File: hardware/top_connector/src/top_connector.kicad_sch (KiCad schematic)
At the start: 13 parts, among them J1 to prev top connector, J2 to next top connector, J3 to module, U1 XL1509-5.0, U2 74LVC1G66

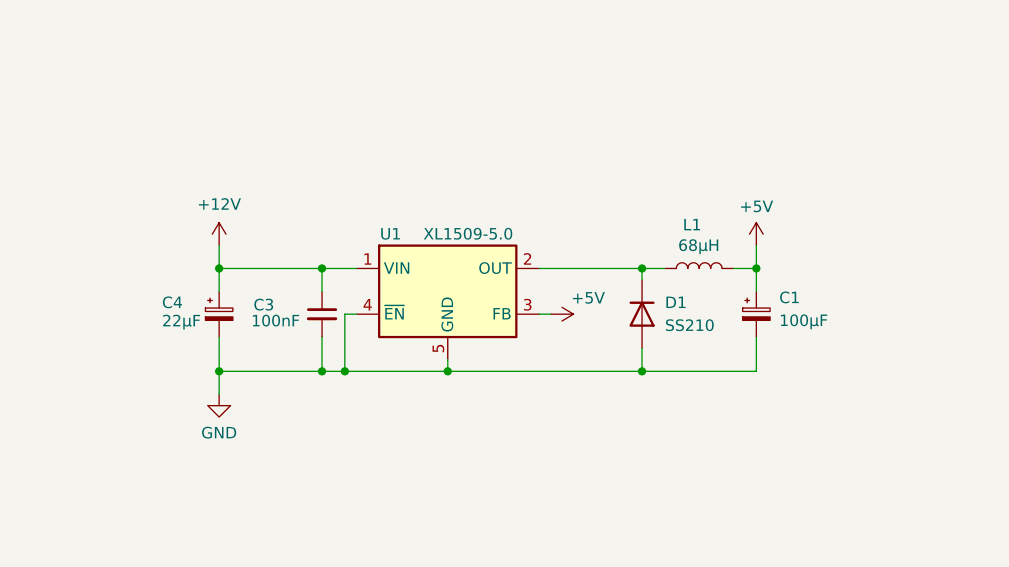
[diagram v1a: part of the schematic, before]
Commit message: Changed micro symbol to uF
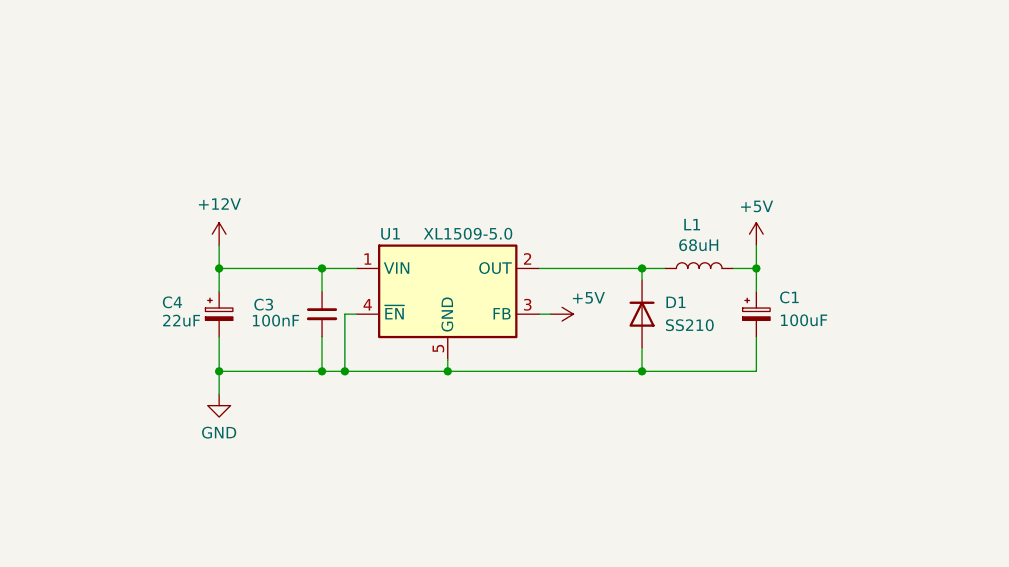
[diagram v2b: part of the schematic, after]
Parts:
- C1: value 100µF -> 100uF
- C4: value 22µF -> 22uF
- L1: value 68µH -> 68uH
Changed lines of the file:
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@@
 		(rev "2.0.1")
 		(company "OpenFlap")
-        (comment 1 "${GIT_TAG}")
+		(comment 1 "${GIT_TAG}")
 		(comment 2 "Repo: github.com/ToonVanEyck/OpenFlap")
 		(comment 3 "Designer: Toon Van Eyck")
@@
 			)
 		)
-		(property "Value" "22µF"
+		(property "Value" "22uF"
 			(at 69.85 201.422 0)
 			(effects
@@
 			)
 		)
-		(property "Value" "68µH"
+		(property "Value" "68uH"
 			(at 131.826 193.04 90)
 			(effects
@@
 			)
 		)
-		(property "Value" "100µF"
+		(property "Value" "100uF"
 			(at 138.43 201.3839 0)
 			(effects

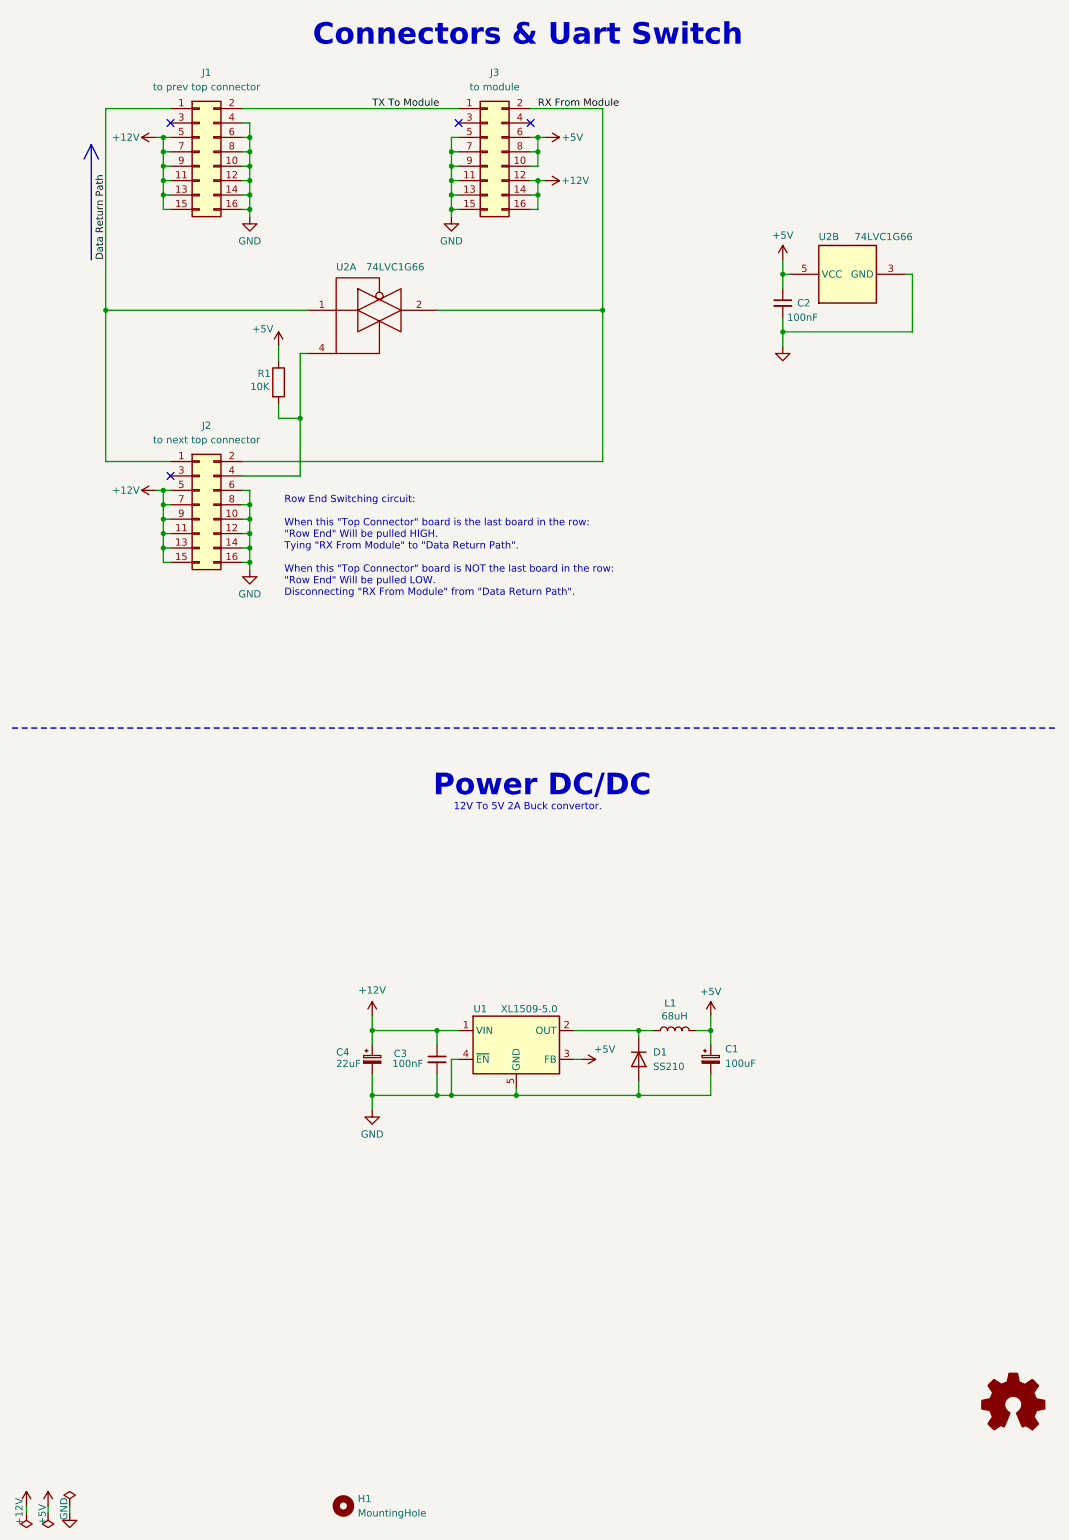
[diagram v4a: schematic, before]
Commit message: Rework top connector and side panel connections to increase power rating. Switch from 2 channel to 4 channel incremental encoder.
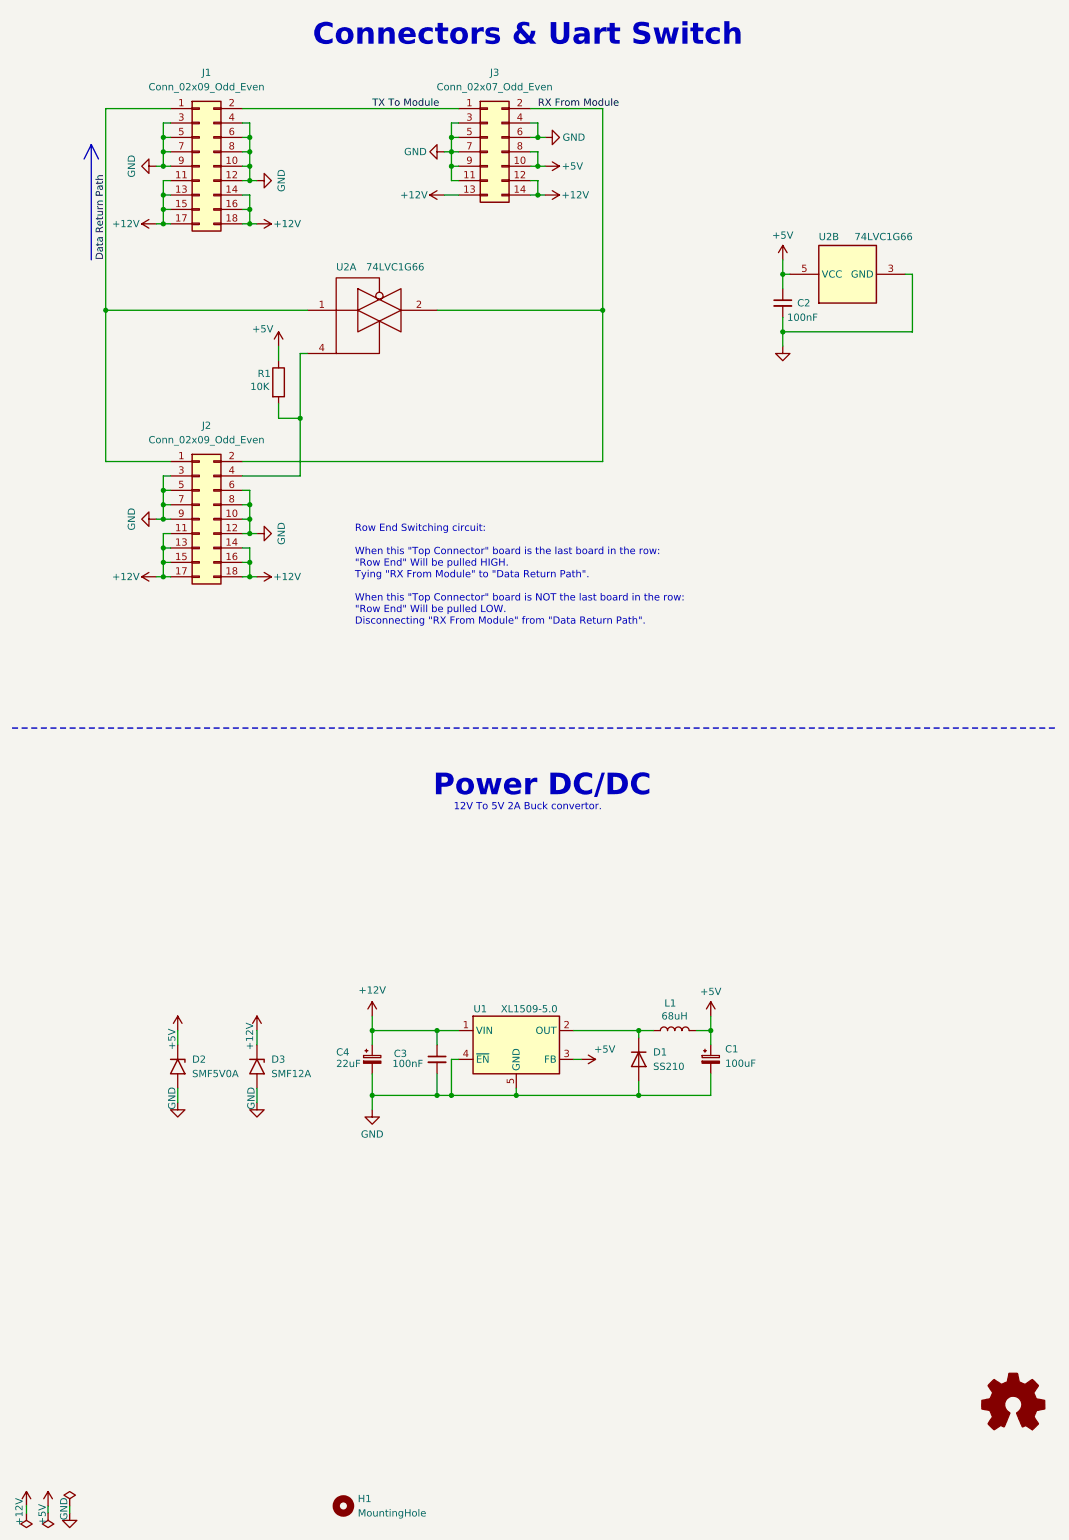
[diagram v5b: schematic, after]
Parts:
- removed J1: to prev top connector, Connector_IDC:IDC-Header_2x08_P2.54mm_Vertical, symbol Connector_Generic:Conn_02x08_Odd_Even
- removed J2: to next top connector, Connector_IDC:IDC-Header_2x08_P2.54mm_Vertical, symbol Connector_Generic:Conn_02x08_Odd_Even
- removed J3: to module, Connector_Samtec_HLE_SMD:Samtec_HLE-108-02-xxx-DV-BE_2x08_P2.54mm_Horizontal, symbol Connector_Generic:Conn_02x08_Odd_Even
- added D2: SMF5V0A, Diode_SMD:D_SMF, symbol Diode:SMF5V0A
- added D3: SMF12A, Diode_SMD:D_SMF, symbol Diode:SMF12A
- added J1, J2: Conn_02x09_Odd_Even, Connector_IDC:IDC-Header_2x09_P2.54mm_Vertical, symbol Connector_Generic:Conn_02x09_Odd_Even
- added J3: Conn_02x07_Odd_Even, Connector_Samtec_HLE_SMD:Samtec_HLE-107-02-xxx-DV-BE-A_2x07_P2.54mm_Horizontal, symbol Connector_Generic:Conn_02x07_Odd_Even
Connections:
- net +12V: now also D3.1 (A1), J1.11 (Pin_11), J1.13 (Pin_13), J1.14 (Pin_14), J1.15 (Pin_15), J1.16 (Pin_16), J1.17 (Pin_17), J1.18 (Pin_18), J2.11 (Pin_11), J2.13 (Pin_13), J2.14 (Pin_14), J2.15 (Pin_15), J2.16 (Pin_16), J2.17 (Pin_17), J2.18 (Pin_18), J3.12 (Pin_12), J3.13 (Pin_13), J3.14 (Pin_14)
- net +5V: now also D2.1 (A1), J3.10 (Pin_10), J3.8 (Pin_8)
- net Data Return Path: now also J1.1 (Pin_1), J2.1 (Pin_1)
- net GND: now also D2.2 (A2), D3.2 (A2), J1.10 (Pin_10), J1.12 (Pin_12), J1.3 (Pin_3), J1.4 (Pin_4), J1.5 (Pin_5), J1.6 (Pin_6), J1.7 (Pin_7), J1.8 (Pin_8), J1.9 (Pin_9), J2.10 (Pin_10), J2.12 (Pin_12), J2.3 (Pin_3), J2.5 (Pin_5), J2.6 (Pin_6), J2.7 (Pin_7), J2.8 (Pin_8), J2.9 (Pin_9), J3.11 (Pin_11), J3.3 (Pin_3), J3.4 (Pin_4), J3.5 (Pin_5), J3.6 (Pin_6), J3.7 (Pin_7), J3.9 (Pin_9)
- net RX From Module: now also J2.2 (Pin_2), J3.2 (Pin_2)
- net TX To Module: now also J1.2 (Pin_2), J3.1 (Pin_1)
- net at R1.2, U2.4: now also J2.4 (Pin_4)
- no-connect marks 4 -> 0

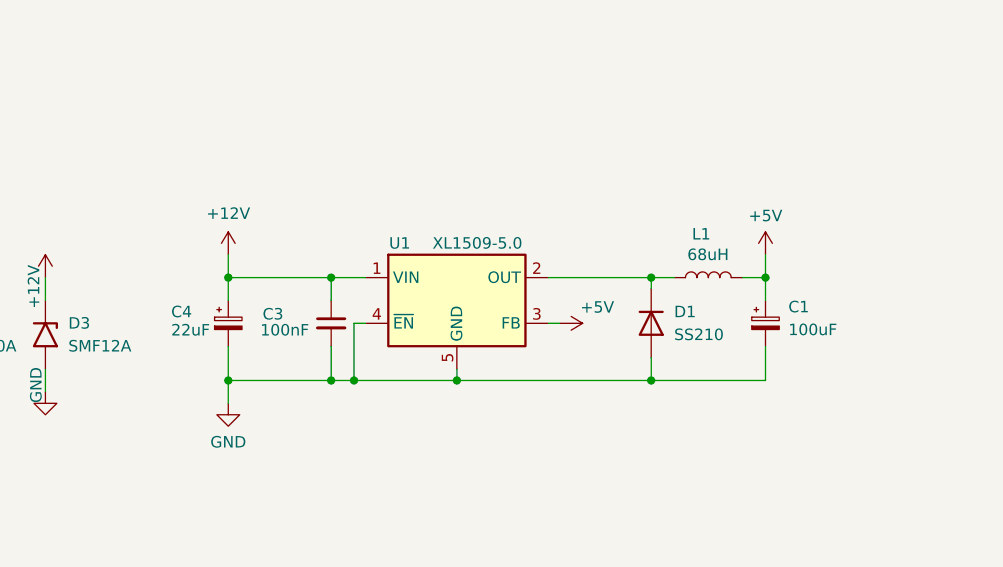
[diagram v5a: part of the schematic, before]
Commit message: Add test points to pcb's
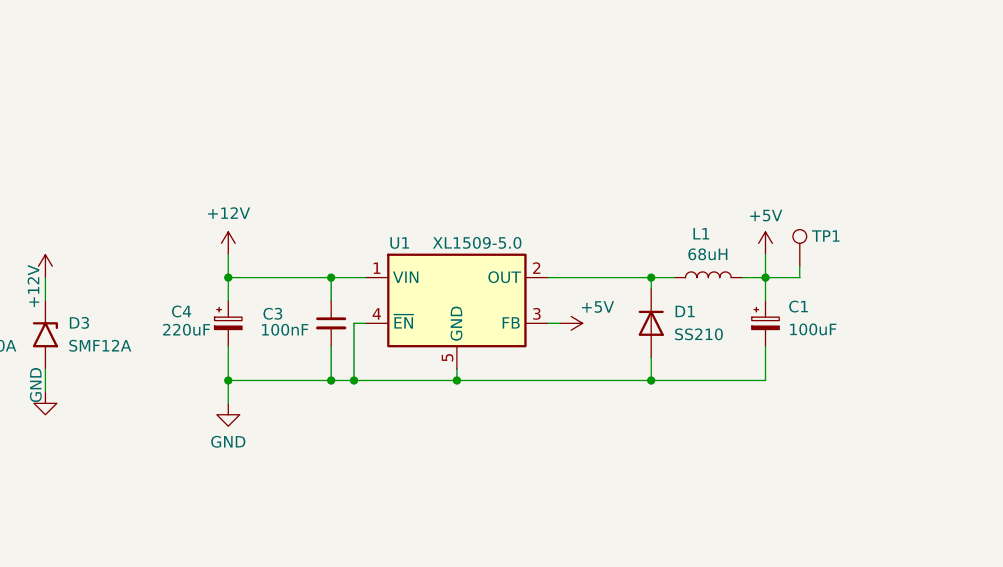
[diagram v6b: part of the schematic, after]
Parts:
- added TP1: TestPoint, TestPoint:TestPoint_Pad_D1.5mm, symbol Connector:TestPoint
- C4: value 22uF -> 220uF; footprint Capacitor_SMD:CP_Elec_5x5.4 -> Capacitor_SMD:CP_Elec_6.3x7.7
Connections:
- net +5V: now also TP1.1
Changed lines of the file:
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@@
 		(title "Top Connector")
 		(date "${DATE}")
-		(rev "3.0.0")
+		(rev "3.0.1")
 		(company "OpenFlap")
 		(comment 1 "${GIT_TAG}")
@@
 	(wire
 		(pts
+			(xy 135.89 193.04) (xy 135.89 195.58)
+		)
+		(stroke
+			(width 0)
+			(type default)
+		)
+	)
+	(wire
+		(pts
 			(xy 40.64 35.56) (xy 39.37 35.56)
 		)
@@
 	(wire
 		(pts
+			(xy 139.7 194.31) (xy 139.7 195.58)
+		)
+		(stroke
+			(width 0)
+			(type default)
+		)
+	)
+	(wire
+		(pts
 			(xy 116.84 95.25) (xy 116.84 68.58)
 		)
@@
 	(wire
 		(pts
-			(xy 90.17 200.66) (xy 90.17 207.01)
+			(xy 139.7 195.58) (xy 135.89 195.58)
 		)
 		(stroke
@@
 	(wire
 		(pts
-			(xy 53.34 40.64) (xy 54.61 40.64)
+			(xy 90.17 200.66) (xy 90.17 207.01)
 		)
 		(stroke
@@
 	(wire
 		(pts
-			(xy 135.89 193.04) (xy 135.89 195.58)
+			(xy 53.34 40.64) (xy 54.61 40.64)
 		)
 		(stroke
@@
 	)
 	(symbol
-		(lib_id "Device:C_Polarized_Small")
-		(at 76.2 200.66 0)
+		(lib_id "Device:C_Small")
+		(at 87.63 200.66 0)
 		(unit 1)
 		(exclude_from_sim no)
@@
 		(on_board yes)
 		(dnp no)
-		(property "Reference" "C4"
-			(at 69.85 199.39 0)
+		(property "Reference" "C3"
+			(at 80.01 199.644 0)
 			(effects
 				(font
@@
 			)
 		)
-		(property "Value" "22uF"
-			(at 69.85 201.422 0)
+		(property "Value" "100nF"
+			(at 79.756 201.422 0)
 			(effects
 				(font
@@
 			)
 		)
-		(property "Footprint" "Capacitor_SMD:CP_Elec_5x5.4"
-			(at 76.2 200.66 0)
+		(property "Footprint" "Capacitor_SMD:C_0805_2012Metric"
+			(at 87.63 200.66 0)
 			(effects
 				(font
@@
 		)
 		(property "Datasheet" "~"
-			(at 76.2 200.66 0)
-			(effects
-				(font
-					(size 1.27 1.27)
-				)
-				(hide yes)
-			)
-		)
-		(property "Description" "Polarized capacitor, small symbol"
-			(at 76.2 200.66 0)
+			(at 87.63 200.66 0)
 			(effects
 				(font
@@
 			)
 		)
-		(property "LCSC" "C280399"
-			(at 76.2 200.66 0)
+		(property "Description" "Unpolarized capacitor, small symbol"
+			(at 87.63 200.66 0)
 			(effects
 				(font
@@
 		)
 		(instances
-			(project ""
+			(project "Top Connector"
 				(path "/af031611-7aa5-43e1-8885-232b80813f15"
-					(reference "C4")
+					(reference "C3")
 					(unit 1)
 				)
@@
 	)
 	(symbol
-		(lib_id "Device:C_Small")
-		(at 87.63 200.66 0)
+		(lib_id "Device:L")
+		(at 129.54 195.58 90)
 		(unit 1)
 		(exclude_from_sim no)
@@
 		(on_board yes)
 		(dnp no)
-		(property "Reference" "C3"
-			(at 80.01 199.644 0)
+		(property "Reference" "L1"
+			(at 129.794 190.754 90)
 			(effects
 				(font
@@
 			)
 		)
-		(property "Value" "100nF"
-			(at 79.756 201.422 0)
+		(property "Value" "68uH"
+			(at 131.826 193.04 90)
 			(effects
 				(font
@@
 			)
 		)
-		(property "Footprint" "Capacitor_SMD:C_0805_2012Metric"
-			(at 87.63 200.66 0)
+		(property "Footprint" "Inductor_SMD:L_Sunlord_SWPA6045S"
+			(at 129.54 195.58 0)
 			(effects
 				(font
@@
 		)
 		(property "Datasheet" "~"
-			(at 87.63 200.66 0)
+			(at 129.54 195.58 0)
 			(effects
 				(font
@@
 			)
 		)
-		(property "Description" "Unpolarized capacitor, small symbol"
-			(at 87.63 200.66 0)
+		(property "Description" "Inductor"
+			(at 129.54 195.58 0)
+			(effects
+				(font
+					(size 1.27 1.27)
+				)
+				(hide yes)
+			)
+		)
+		(property "LCSC" "C53663"
+			(at 129.54 195.58 90)
 			(effects
 				(font
@@
 		)
 		(instances
-			(project "Top Connector"
+			(project ""
 				(path "/af031611-7aa5-43e1-8885-232b80813f15"
-					(reference "C3")
+					(reference "L1")
 					(unit 1)
 				)
@@
 	)
 	(symbol
-		(lib_id "Device:L")
-		(at 129.54 195.58 90)
+		(lib_id "Device:C_Polarized_Small")
+		(at 76.2 200.66 0)
 		(unit 1)
 		(exclude_from_sim no)
@@
 		(on_board yes)
 		(dnp no)
-		(property "Reference" "L1"
-			(at 129.794 190.754 90)
+		(property "Reference" "C4"
+			(at 69.85 199.39 0)
 			(effects
 				(font
@@
 			)
 		)
-		(property "Value" "68uH"
-			(at 131.826 193.04 90)
+		(property "Value" "220uF"
+			(at 68.834 201.422 0)
 			(effects
 				(font
@@
 			)
 		)
-		(property "Footprint" "Inductor_SMD:L_Sunlord_SWPA6045S"
-			(at 129.54 195.58 0)
+		(property "Footprint" "Capacitor_SMD:CP_Elec_6.3x7.7"
+			(at 76.2 200.66 0)
 			(effects
 				(font
@@
 		)
 		(property "Datasheet" "~"
-			(at 129.54 195.58 0)
+			(at 76.2 200.66 0)
 			(effects
 				(font
@@
 			)
 		)
-		(property "Description" "Inductor"
-			(at 129.54 195.58 0)
+		(property "Description" "Polarized capacitor, small symbol"
+			(at 76.2 200.66 0)
 			(effects
 				(font
@@
 			)
 		)
-		(property "LCSC" "C53663"
-			(at 129.54 195.58 90)
+		(property "LCSC" "C280399"
+			(at 76.2 200.66 0)
 			(effects
 				(font
@@
 		)
 		(instances
-			(project ""
+			(project "top_connector"
 				(path "/af031611-7aa5-43e1-8885-232b80813f15"
-					(reference "L1")
+					(reference "C4")
 					(unit 1)
 				)
@@
 					(unit 1)
 				)
+			)
+		)
+	)
+	(symbol
+		(lib_id "Connector:TestPoint")
+		(at 139.7 194.31 0)
+		(mirror y)
+		(unit 1)
+		(exclude_from_sim no)
+		(in_bom yes)
+		(on_board yes)
+		(dnp no)
+		(property "Reference" "TP1"
+			(at 144.272 191.008 0)
+			(effects
+				(font
+					(size 1.27 1.27)
+				)
+				(justify left)
+			)
+		)
+		(property "Value" "TestPoint"
+			(at 138.43 189.23 90)
+			(effects
+				(font
+					(size 1.27 1.27)
+				)
+				(justify left)
+				(hide yes)
+			)
+		)
+		(property "Footprint" "TestPoint:TestPoint_Pad_D1.5mm"
+			(at 134.62 194.31 0)
+			(effects
+				(font
+					(size 1.27 1.27)
+				)
+				(hide yes)
+			)
+		)
+		(property "Datasheet" "~"
+			(at 134.62 194.31 0)
+			(effects
+				(font
+					(size 1.27 1.27)
+				)
+				(hide yes)
+			)
+		)
+		(property "Description" "test point"
+			(at 139.7 194.31 0)
+			(effects
+				(font
+					(size 1.27 1.27)
+				)
+				(hide yes)
+			)
+		)
+		(pin "1"
+		)
+		(instances
+			(project "top_connector"
+				(path "/af031611-7aa5-43e1-8885-232b80813f15"
+					(reference "TP1")
+					(unit 1)
+				)
